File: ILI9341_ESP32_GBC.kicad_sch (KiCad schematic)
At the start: 98 parts, among them CN2 PJ-3043-B, J1 USB_C_Receptacle_USB2.0_16P, Q3 BC817, Q7 PMOS, Q8 PMOS, SW6 K3-1290S-J1, SW7 SW_Push, SW8 SW_Push, U1 CH340N, U11 ESP32-WROVER-E-N8R8, U2 XM5062S, U4 BQ25171QWDRCRQ1, U7 02FVS3, U8 PAM8406D, U9 TPS61028DRCR

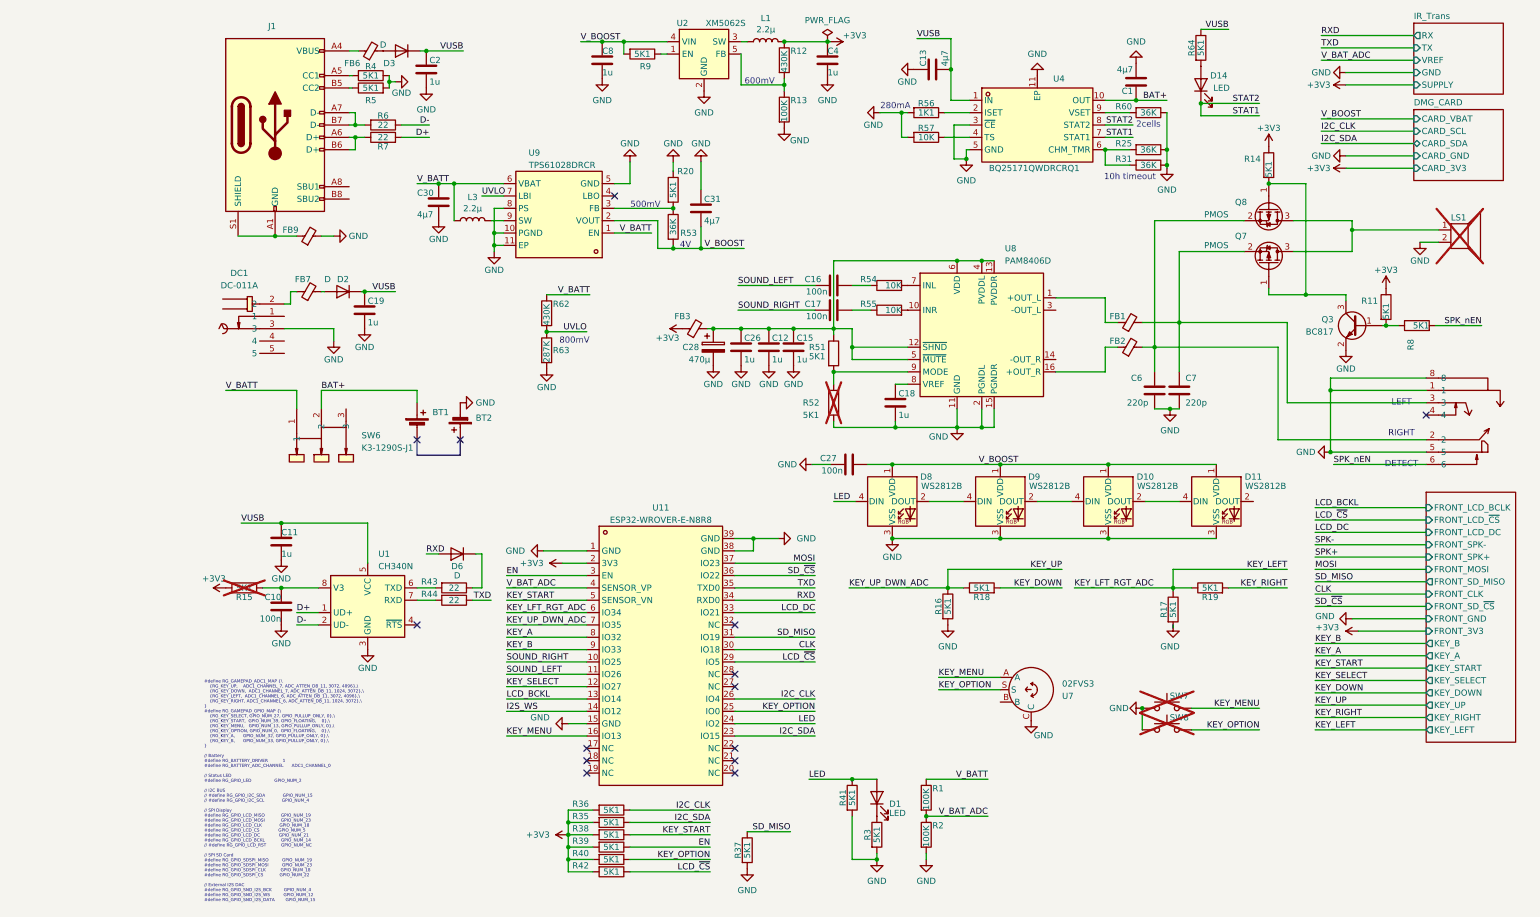
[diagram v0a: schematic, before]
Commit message: update online version before change to esp32 s3
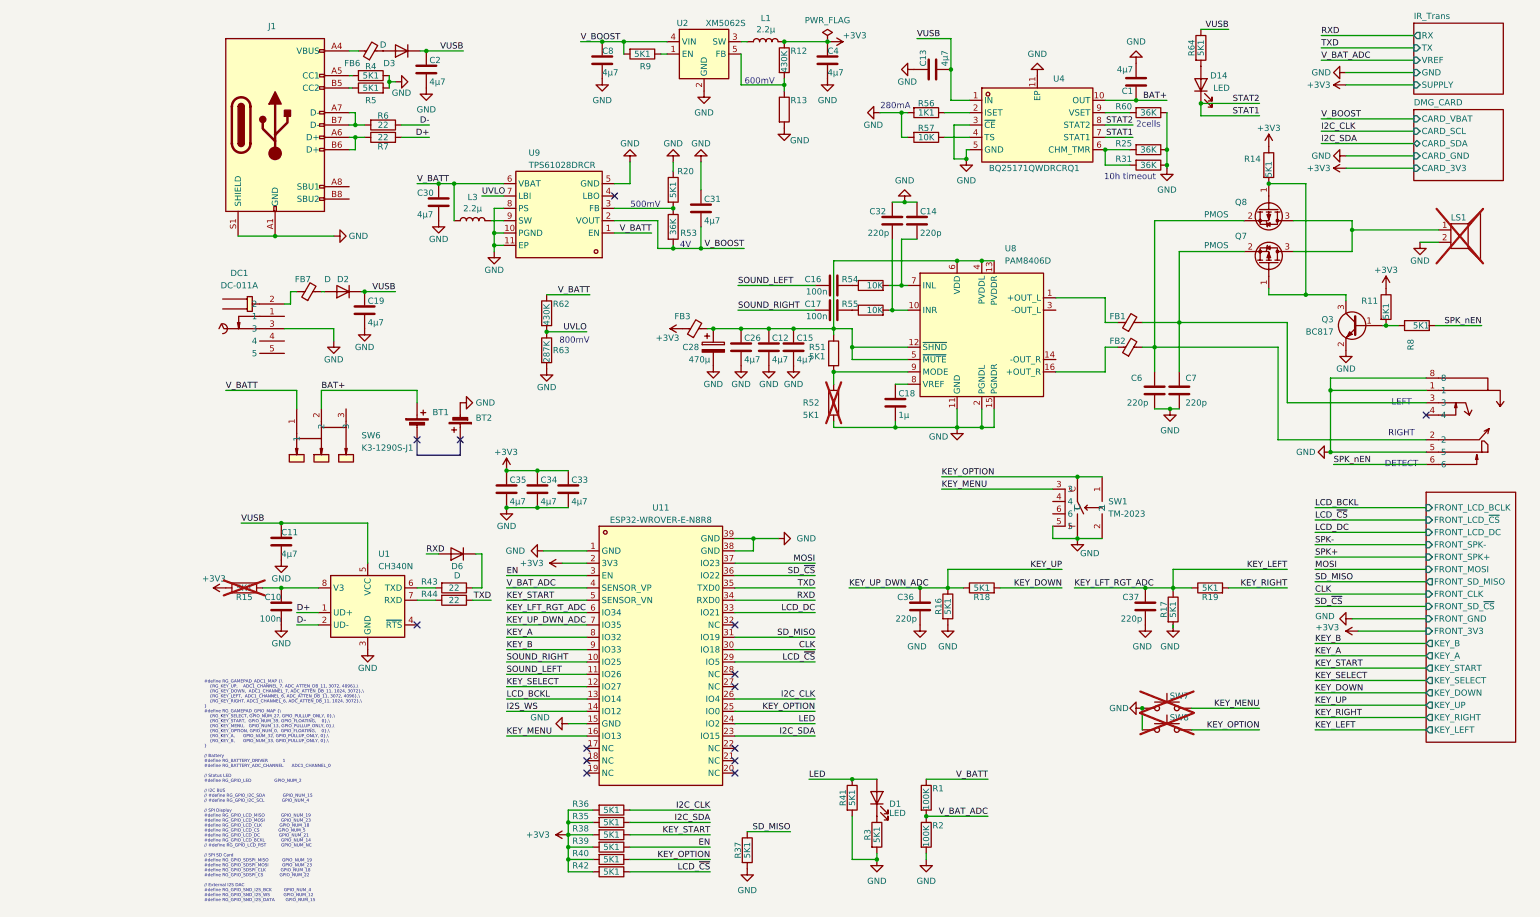
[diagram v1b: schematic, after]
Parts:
- removed C27: 100n, Capacitor_SMD:C_0603_1608Metric, symbol Device:C
- removed D10, D11, D8, D9: WS2812B, LED_SMD:LED_WS2812B_PLCC4_5.0x5.0mm_P3.2mm, symbol LED:WS2812B
- removed FB9: FerriteBead_Small, Inductor_SMD:L_0805_2012Metric, symbol Device:FerriteBead_Small
- removed U7: 02FVS3, TheBrutzlers_Lib:02FVS3, symbol theBrutzler:02FVS3
- added C14, C32, C36, C37: 220p, Capacitor_SMD:C_0603_1608Metric, symbol Device:C
- added C33, C34, C35: 4µ7, Capacitor_SMD:C_0603_1608Metric, symbol Device:C
- added SW1: TM-2023, easyeda2kicad:SW-SMD_TM-2023-1, symbol easyeda2kicad:TM-2023
- BT1: footprint TheBrutzlers_Lib:BATTERY_AA_SMD_PLUS -> easyeda2kicad:CONN-SMD_MY-ZJ-3030
- BT2: footprint TheBrutzlers_Lib:NINTENDO_MINUS -> easyeda2kicad:BAT-SMD_MY-FJ-3031
- C1, C13, C30, C31: footprint Capacitor_SMD:C_1206_3216Metric -> Capacitor_SMD:C_0603_1608Metric; LCSC C282809 -> C69335
- C11, C12, C15, C19, C2, C26, C4, C8: value 1u -> 4µ7; LCSC C5673 -> C69335
- C18: value 1u -> 1µ
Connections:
- net +3V3: now also C33.1, C34.1, C35.1
- net GND: now also J1.A1 (GND), J1.A12 (GND), J1.B1 (GND), J1.B12 (GND), J1.S1 (SHIELD), C14.2, C32.1, C33.2, C34.2, C35.2, C36.2, C37.2, SW1.2, SW1.5, SW1.T
- net KEY_LEFT: now also C37.1
- net KEY_MENU: now also SW1.3
- net KEY_OPTION: now also SW1.1, SW1.C
- net KEY_UP: now also C36.1
- net at R55.2, U8.10 (INR): now also C32.2
- net at R54.2, U8.7 (INL): now also C14.1
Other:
- moved on the sheet: R54, R55

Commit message: updated version with esp32 s3 and i2s audio ic
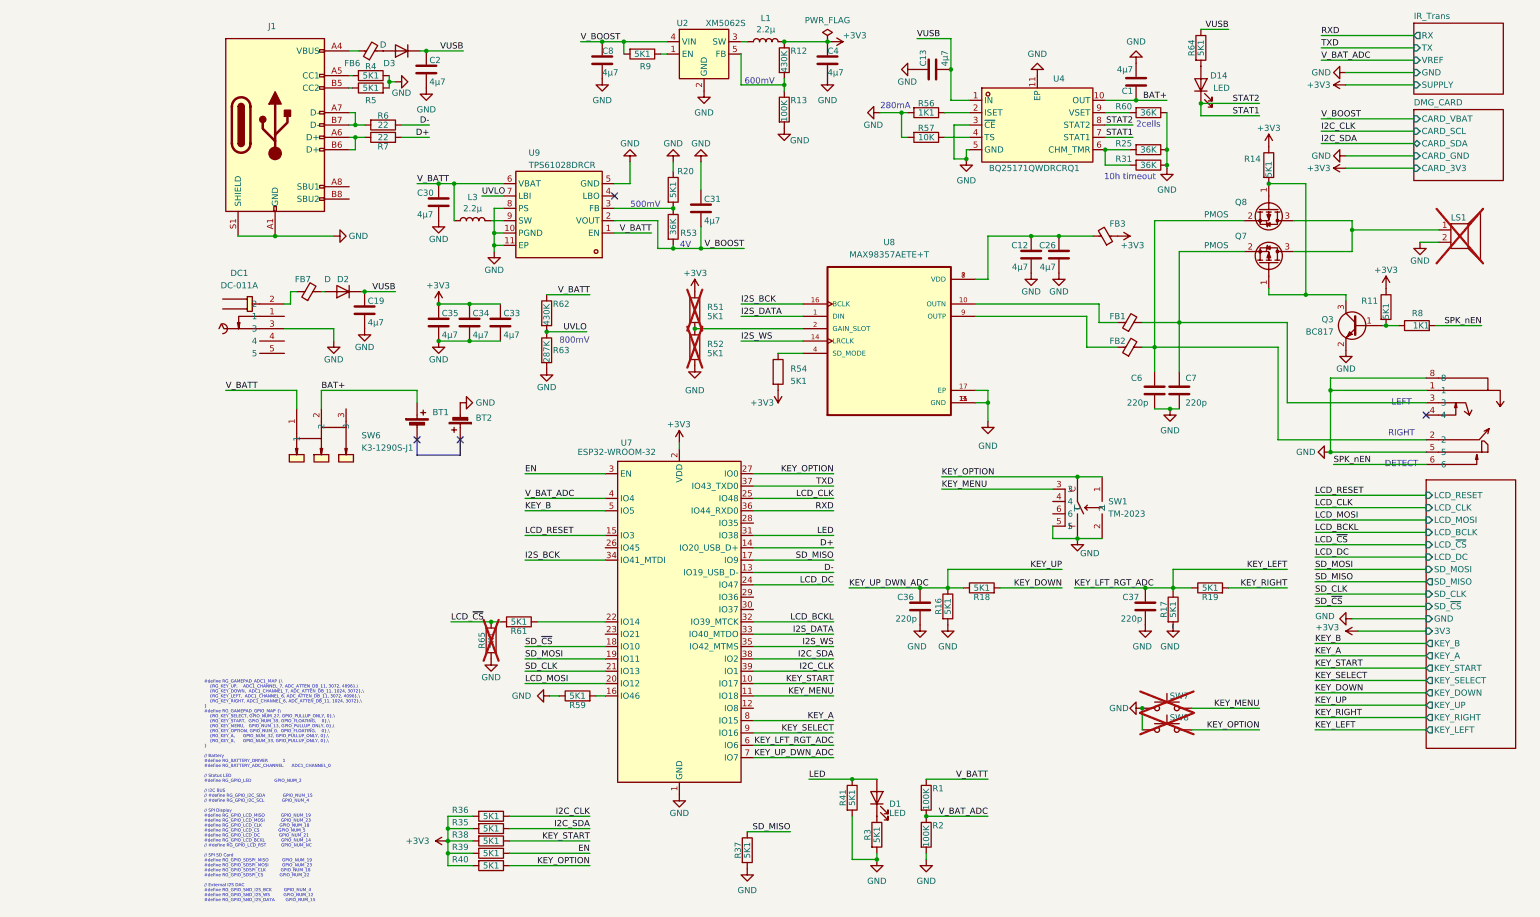
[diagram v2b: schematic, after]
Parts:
- removed C10, C16, C17: 100n, Capacitor_SMD:C_0603_1608Metric, symbol Device:C
- removed C11, C15: 4µ7, Capacitor_SMD:C_0603_1608Metric, symbol Device:C
- removed C14, C32: 220p, Capacitor_SMD:C_0603_1608Metric, symbol Device:C
- removed C18: 1µ, Capacitor_SMD:C_0603_1608Metric, symbol Device:C
- removed C28: 470µ, Capacitor_Tantalum_SMD:CP_EIA-7343-43_Kemet-X, symbol Device:C_Polarized
- removed D6: D, Diode_SMD:Nexperia_CFP3_SOD-123W, symbol Device:D
- removed R15, R42: 5K1, Resistor_SMD:R_0603_1608Metric, symbol Device:R
- removed R43, R44: 22, Resistor_SMD:R_0603_1608Metric, symbol Device:R
- removed R55: 10K, Resistor_SMD:R_0603_1608Metric, symbol Device:R
- removed U1: CH340N, Package_SO:SOP-8_3.9x4.9mm_P1.27mm, symbol Interface_USB:CH340N
- removed U11: ESP32-WROVER-E-N8R8, easyeda2kicad:WIFI-SMD_ESP32-WROVER-IE8MB, symbol easyeda2kicad:ESP32-WROVER-E-N8R8
- removed U8: PAM8406D, Package_SO:SOP-16_3.9x9.9mm_P1.27mm, symbol Amplifier_Audio:PAM8406D
- added R59, R61, R65: 5K1, Resistor_SMD:R_0603_1608Metric, symbol Device:R
- added U7: ESP32-WROOM-32, TheBrutzlers_Lib:ESP32-S3-WROOM-1, symbol theBrutzler:ESP32-S3-WROOM-N16R8
- added U8: MAX98357AETE+T, Package_DFN_QFN:QFN-16-1EP_3x3mm_P0.5mm_EP1.45x1.45mm, symbol MAX98357AETE_T:MAX98357AETE+T
- R51: SOURCED ok -> (none); now not fitted; now left out of the parts list
- R52: SOURCED ok -> (none)
- R54: value 10K -> 5K1; LCSC C25804 -> C26000; SOURCED ok -> (none)
- R8: value 5K1 -> 1K1; LCSC C26000 -> C2906975
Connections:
- net +3V3: now also R51.1, R54.2, U7.2 (VDD)
- net D+: now also U7.14 (IO20_USB_D+)
- net D-: now also U7.13 (IO19_USB_D-)
- net EN: now also U7.3 (EN)
- net GND: now also R59.1, R65.1, U7.1 (GND), U7.40 (GND), U7.41 (GND), U8.11 (GND), U8.15 (GND), U8.17 (EP), U8.3 (GND)
- net I2C_CLK: now also U7.39 (IO1)
- net I2C_SDA: now also U7.38 (IO2)
- net I2S_WS: now also U7.35 (IO42_MTMS), U8.14 (LRCLK)
- net KEY_A: now also U7.8 (IO15)
- net KEY_B: now also U7.5 (IO5)
- net KEY_LEFT: now also U7.6 (IO6)
- net KEY_MENU: now also U7.11 (IO18)
- net KEY_OPTION: now also U7.27 (IO0)
- net KEY_SELECT: now also U7.9 (IO16)
- net KEY_START: now also U7.10 (IO17)
- net KEY_UP: now also U7.7 (IO7)
- net LCD_BCKL: now also U7.32 (IO39_MTCK)
- net LCD_DC: now also U7.24 (IO47)
- net LCD_~{CS}: now also R61.2, R65.2
- net LED: now also U7.31 (IO38)
- net RXD: now also U7.36 (IO44_RXD0)
- net SD_MISO: now also U7.17 (IO9)
- net SD_~{CS}: now also U7.18 (IO10)
- net TXD: now also U7.37 (IO43_TXD0)
- net V_BAT_ADC: now also U7.4 (IO4)
- net at FB2.1: now also U8.9 (OUTP)
- net at C12.1, C26.1, FB3.2: now also U8.7 (VDD), U8.8 (VDD); no longer R51.1
- net at R51.2, R52.1: now also U8.2 (GAIN_SLOT)
- net at R54.1: now also U8.4 (SD_MODE)
- net at FB1.1: now also U8.10 (OUTN)
- new net: R59.2, U7.16 (IO46)
- new net: R61.1, U7.22 (IO14)
- new net I2S_BCK: U7.34 (IO41_MTDI), U8.16 (BCLK)
- new net I2S_DATA: U7.33 (IO40_MTDO), U8.1 (DIN)
- new net LCD_CLK: U7.25 (IO48)
- new net LCD_MOSI: U7.20 (IO12)
- new net LCD_RESET: U7.15 (IO3)
- new net SD_CLK: U7.21 (IO13)
- new net SD_MOSI: U7.19 (IO11)
- no-connect marks 14 -> 4
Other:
- sheet FRONT_BUTTONS ports: added 3V3, GND, LCD_BCLK, LCD_CLK, LCD_DC, LCD_MOSI, LCD_RESET, LCD_~{CS}, SD_CLK, SD_MISO, SD_MOSI, SD_~{CS}; removed FRONT_3V3, FRONT_CLK, FRONT_GND, FRONT_LCD_BCLK, FRONT_LCD_DC, FRONT_LCD_~{CS}, FRONT_MOSI, FRONT_SD_MISO, FRONT_SD_~{CS}, FRONT_SPK+, FRONT_SPK-
- moved on the sheet: C12, C26, C33, C34, C35, FB3, R35, R36, R38, R39, R40

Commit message: Order V1
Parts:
- removed CN2: PJ-3043-B, easyeda2kicad:AUDIO-TH_PJ-3043-B, symbol easyeda2kicad:PJ-3043-B
- removed Q3: BC817, Package_TO_SOT_SMD:SOT-323_SC-70, symbol Transistor_BJT:BC817
- removed Q7, Q8: PMOS, Package_TO_SOT_SMD:SOT-323_SC-70, symbol Device:Q_PMOS_GSD
- removed R11, R14, R41: 5K1, Resistor_SMD:R_0603_1608Metric, symbol Device:R
- added Audio1: PJ-3537-X, easyeda2kicad:AUDIO-SMD_PJ-3420-A-SMT_C319102, symbol easyeda2kicad:PJ-3537-X
- added D5: LED, LED_SMD:LED_0603_1608Metric, symbol Device:LED
- added J2: Conn_01x05_Pin, Connector_PinHeader_2.54mm:PinHeader_1x05_P2.54mm_Vertical, symbol Connector:Conn_01x05_Pin
- added R26: 5K1, Resistor_SMD:R_0603_1608Metric, symbol Device:R
- D1, R61: now not fitted; now left out of the parts list
- D14: footprint LED_THT:LED_D3.0mm_FlatTop -> LED_SMD:LED_0603_1608Metric; LCSC C440523 -> C7496818
- R20: value 5K1 -> 1K1; LCSC C26000 -> C2906975
- R53: value 36K -> 10K; LCSC C23147 -> C25804
- R65: now fitted; now in the parts list
- R8: value 1K1 -> 5K1; LCSC C2906975 -> C26000
- U4: LCSC Part (none) -> C2861221
- U7: value ESP32-WROOM-32 -> ESP32-S3-WROOM-1-N16R8; LCSC C2913201 -> C2913202
- renumbered R56 to R11
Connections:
- net SPK_nEN is gone; now on net +3V3: R8.2
- net +3V3: now also J2.2 (Pin_2)
- net GND: now also SW1.3, SW1.4, SW1.6, SW1.C, Audio1.1, Audio1.2, J2.1 (Pin_1), R26.1; no longer LS1.2, SW1.2, SW1.T
- net I2C_CLK: now also J2.4 (Pin_4)
- net I2C_SDA: now also J2.3 (Pin_3)
- net KEY_MENU: now also SW1.2; no longer SW1.3
- net KEY_OPTION: now also U7.12 (IO8); no longer R40.1, SW1.C, U7.27 (IO0)
- net LCD_RESET: now also R8.1
- net LED: now also D5.2 (A)
- net V_BOOST: now also J2.5 (Pin_5)
- net at C6.1, FB2.2: now also Audio1.3
- net at U7.26 (IO45): now also R26.2
- net at D1.1 (K), R3.1: now also D5.1 (K)
- net at C7.2, FB1.2: now also Audio1.4
- net at LS1.1: now also Audio1.5
- new net: Audio1.6, LS1.2
- new net KEY_BOOT: R40.1, SW1.T, U7.27 (IO0)
- no-connect marks 4 -> 3
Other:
- removed sheet DMG_CARD
- note added: "#define RG_GAMEPAD_ADC1_MAP {\ {RG_KEY_UP, ADC1_CHANNEL_6, ADC_ATTEN_DB_11, 3072, 4096},\ {RG_KEY_DOWN, ADC1_CHANNEL_6, ADC_ATTEN_DB_11, 1024, 3072},\ {RG_KEY_LEFT, ADC1_CHANNEL_5, ADC_ATTEN_DB_11, 3072, 4096},\ {RG_KEY_RIGHT, ADC1_CHANNEL_5, ADC_ATTEN_DB_11, 1024, 3072},\ } #define RG_GAMEPAD_GPIO_MAP {\ {RG_KEY_SELECT, GPIO_NUM_16, GPIO_PULLUP_ONLY, 0},\ {RG_KEY_START, GPIO_NUM_17, GPIO_PULLUP_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"
- note added: "5V"
- note removed: "#define RG_GAMEPAD_ADC1_MAP {\ {RG_KEY_UP, ADC1_CHANNEL_7, ADC_ATTEN_DB_11, 3072, 4096},\ {RG_KEY_DOWN, ADC1_CHANNEL_7, ADC_ATTEN_DB_11, 1024, 3072},\ {RG_KEY_LEFT, ADC1_CHANNEL_6, ADC_ATTEN_DB_11, 3072, 4096},\ {RG_KEY_RIGHT, ADC1_CHANNEL_6, ADC_ATTEN_DB_11, 1024, 3072},\ } #define RG_GAMEPAD_GPIO_MAP {\ {RG_KEY_SELECT, GPIO_NUM_27, GPIO_PULLUP_ONLY, 0},\ {RG_KEY_START, GPIO_NUM_39, GPIO_FLOATIN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"
- note removed: "4V"
- note removed: "DETECT"
- moved on the sheet: FB3

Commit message: update pcb and upload schematic
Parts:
- C36, C37: now not fitted; now left out of the parts list
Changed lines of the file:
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@@
 		(unit 1)
 		(exclude_from_sim no)
-		(in_bom yes)
+		(in_bom no)
 		(on_board yes)
-		(dnp no)
+		(dnp yes)
 		(property "Reference" "C37"
 			(at 206.375 133.985 0)
@@
 		(unit 1)
 		(exclude_from_sim no)
-		(in_bom yes)
+		(in_bom no)
 		(on_board yes)
-		(dnp no)
+		(dnp yes)
 		(property "Reference" "C36"
 			(at 160.02 133.985 0)
